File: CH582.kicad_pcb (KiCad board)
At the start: 2 copper layers, 32 x 32 mm, 48 parts, among them J1 Conn_01x02, J3 USB, J4 Conn_02x04_Odd_Even, J5 Pogo Pin Socket 2.54, Q1 NPN, U2 TP4056, U4 M3406, Y1 32MHz, Y2 Crystal_Small

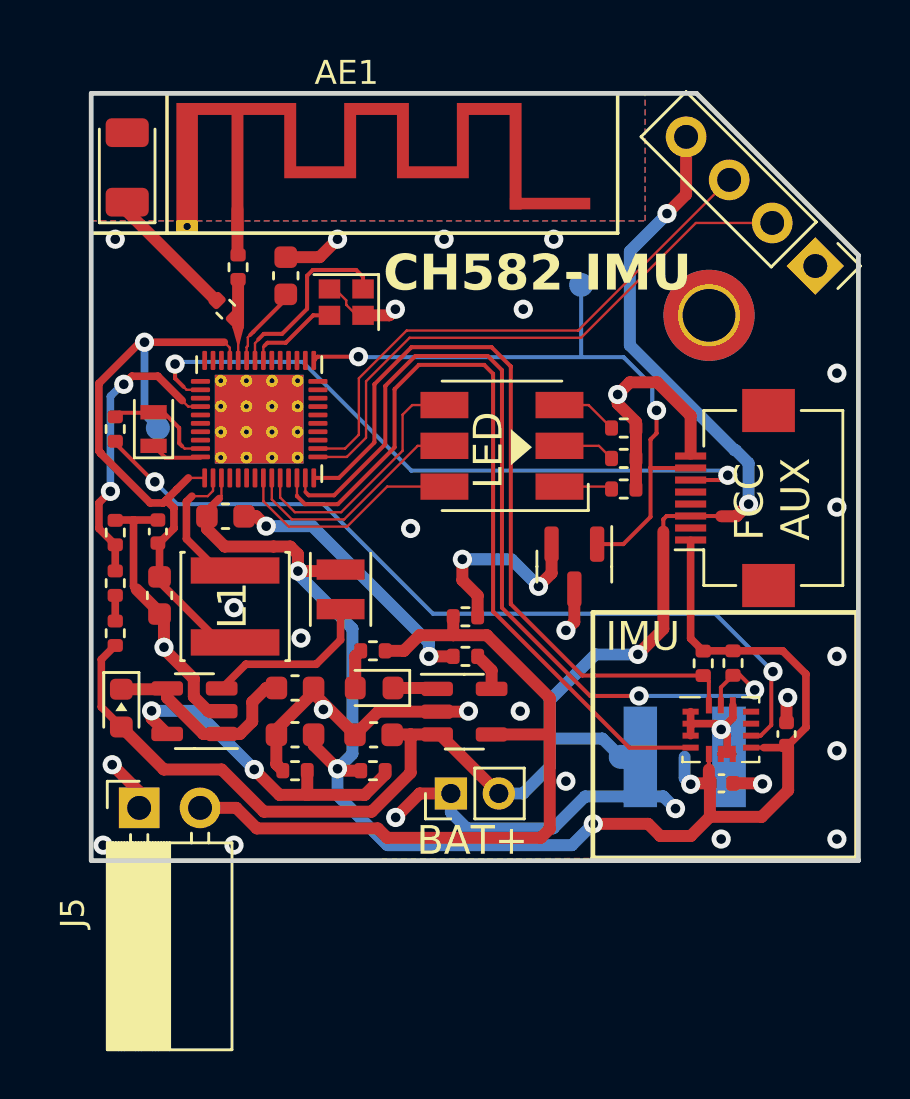
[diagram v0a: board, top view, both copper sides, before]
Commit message: goodbye 0.1mm
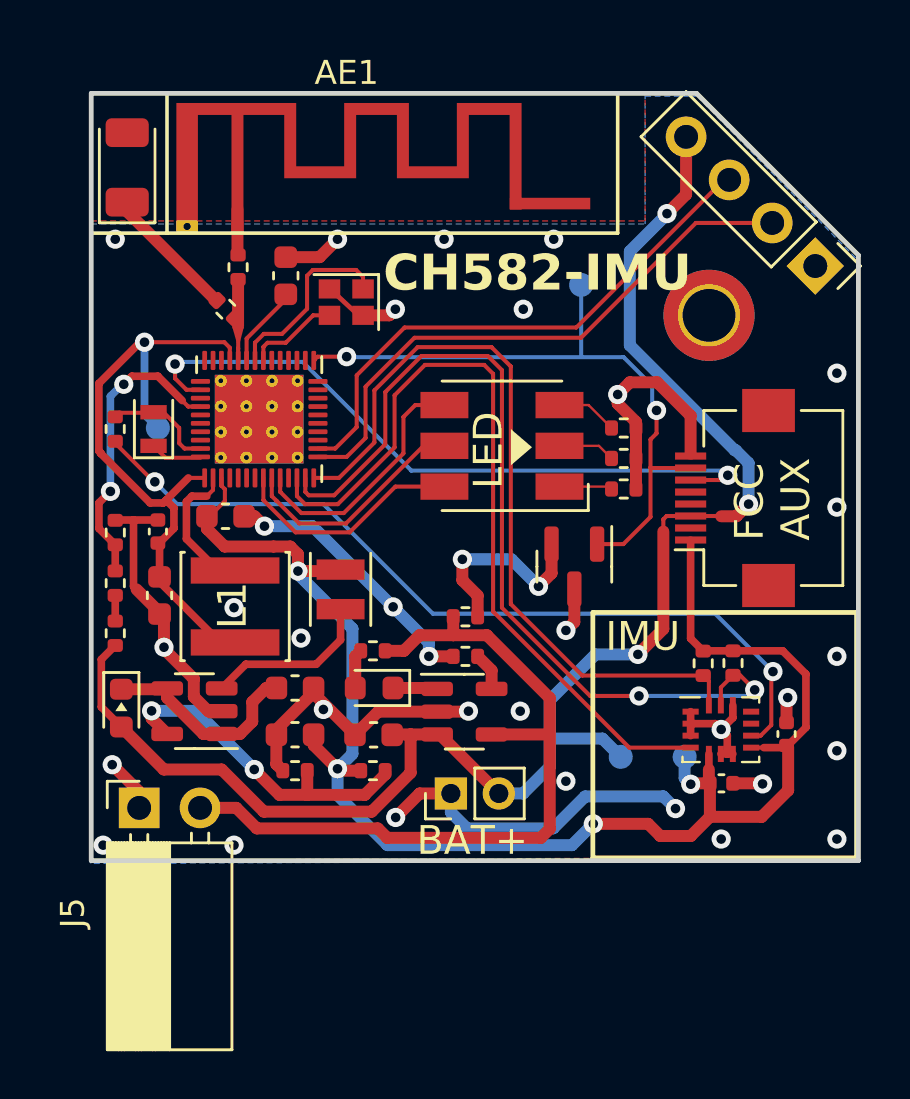
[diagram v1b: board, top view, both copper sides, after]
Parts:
- 3V1: footprint Inductor_SMD:L_Changjiang_FNR5020S -> TestPoint:TestPoint_Pad_D1.0mm
- Q1: value NPN -> NPN, N.C.
- R1: value ? -> N.C.
